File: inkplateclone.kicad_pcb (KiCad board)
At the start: 2 copper layers, 92 parts, among them J1 ED060SC7, J2 USB_C_Receptacle_USB2.0, J3 Conn_01x03_Male, J4 Conn_01x03_Male, J5 Conn_01x02_Male, Q1 Q_NMOS_GSD, Q2 Q_NMOS_GSD, Q3 Q_PMOS_GSD, SW1 SW_Push, SW2 SW_Push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

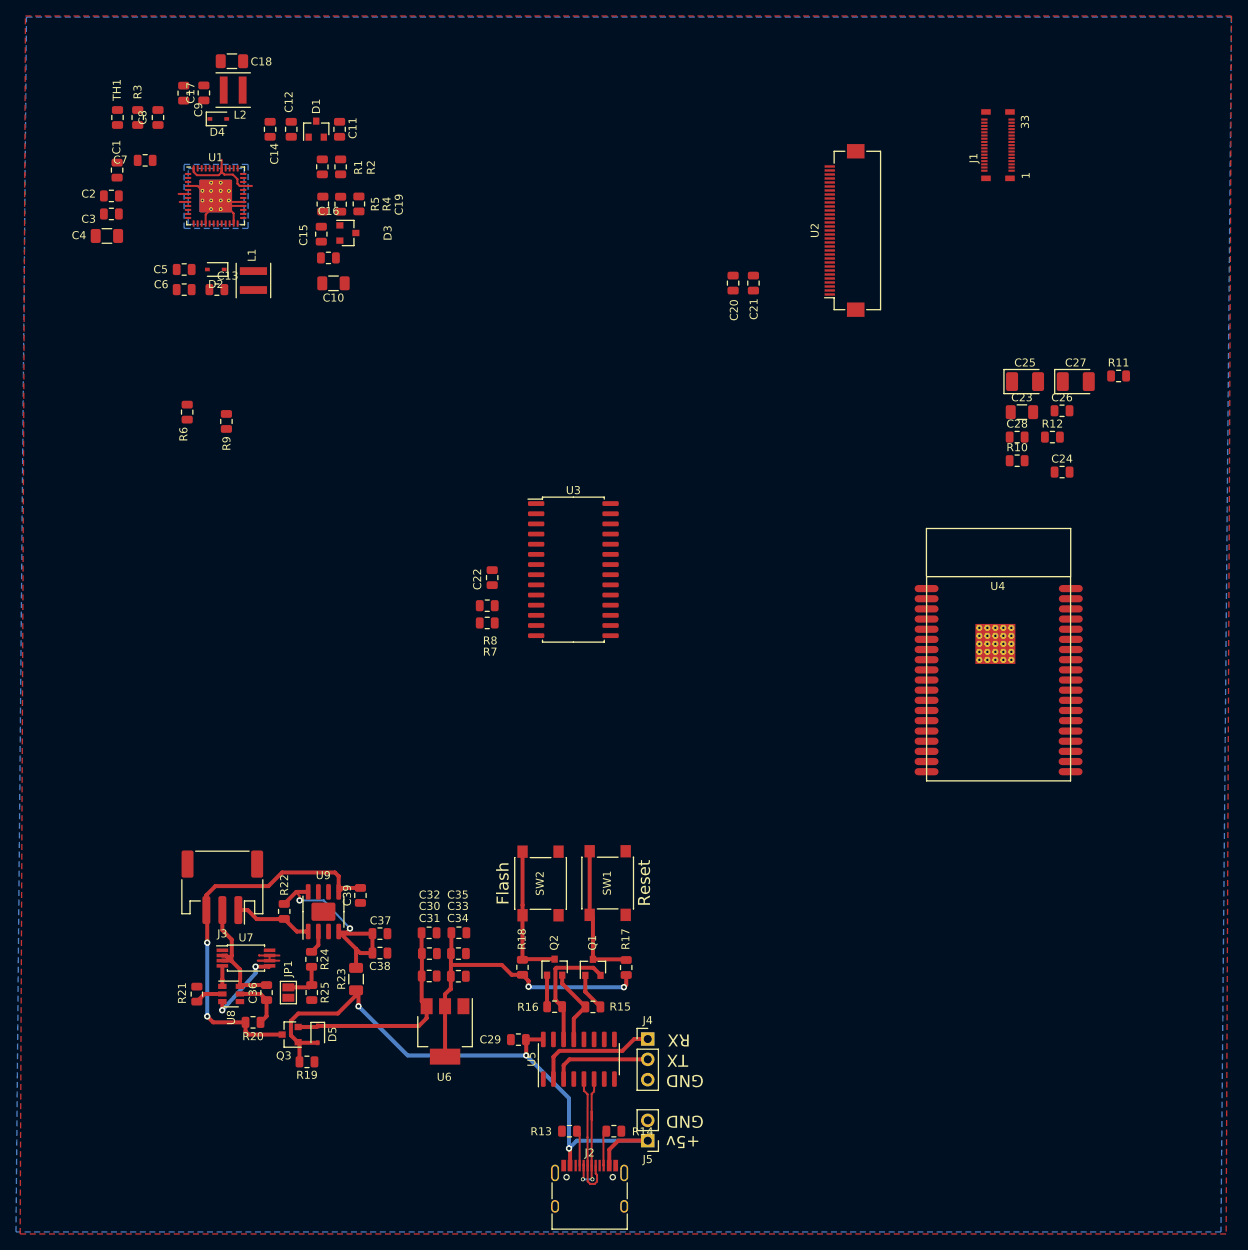
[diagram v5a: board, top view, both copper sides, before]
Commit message: added 3d models for the connectors. Not satisfied but they will do for now.
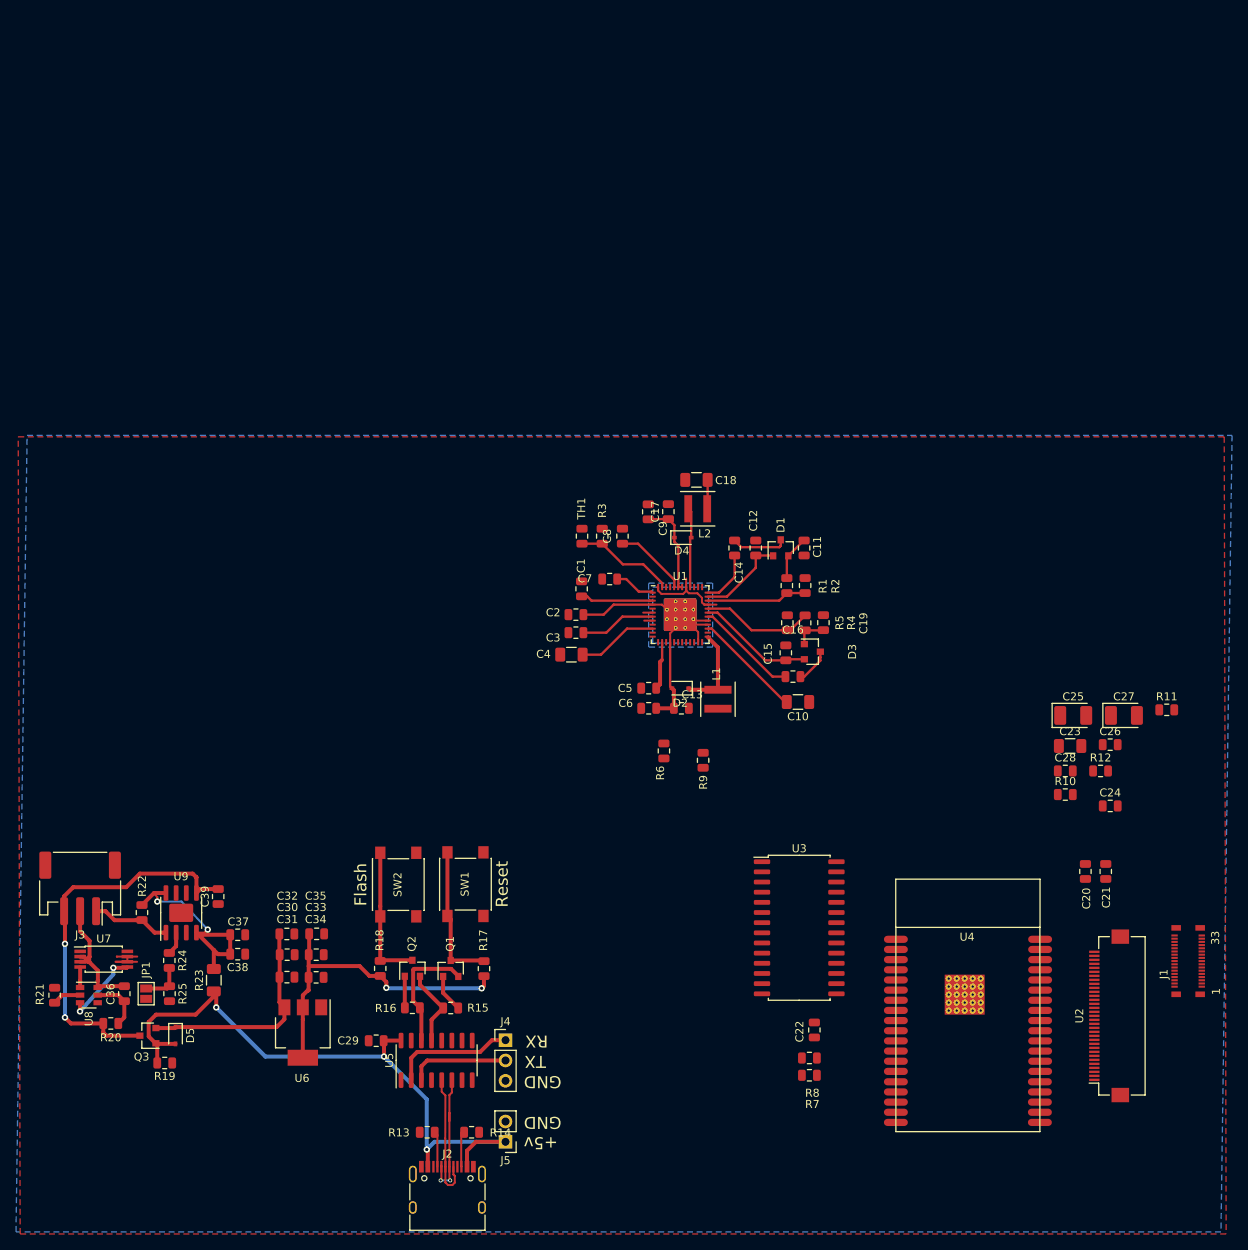
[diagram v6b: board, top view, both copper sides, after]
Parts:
- moved J1 104.7 mm to (186.7, 153.6)
- moved U2 103.6 mm to (176.9, 160.4)
- moved C20 85.7 mm to (173.9, 142.4)
- moved C21 85.7 mm to (176.4, 142.4)
- moved C10 78.2 mm to (138.0, 121.2)
- moved C11 78.2 mm to (138.7, 101.9)
- moved C12 78.2 mm to (130.0, 101.9)
- moved C14 78.2 mm to (132.7, 101.9)
- moved C17 78.2 mm to (121.8, 97.4)
- moved C3 78.2 mm to (110.2, 112.5)
- moved C7 78.2 mm to (114.4, 105.8)
- moved C9 78.2 mm to (119.3, 97.4)
- moved D3 78.2 mm to (139.8, 114.9)
- moved L1 78.2 mm to (128.0, 120.8)
- moved L2 78.2 mm to (125.4, 97.0)
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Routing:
- net VIN: track 27.5 -> 54.9 mm
- net /VN: track 13.0 -> 32.8 mm
- net /VEE_D: track 0.00 -> 14.6 mm
- net /VEE_FB: track 0.00 -> 14.1 mm
- net /VEE_DRV: track 0.00 -> 12.8 mm
- net /VDDH_FB: track 0.00 -> 12.6 mm
- net /TS: track 0.00 -> 12.5 mm
- net /VB: track 0.00 -> 12.0 mm
- net /VDDH_D: track 0.00 -> 11.2 mm
- net /VN_SW: track 0.00 -> 10.8 mm
- net /VB_SW: track 0.00 -> 9.99 mm
- net /INT_LDO: track 0.00 -> 9.47 mm
- net /VPOS: track 0.00 -> 9.27 mm
- net /VNEG: track 0.00 -> 9.09 mm
- net Net-(C12-Pad1): track 0.00 -> 6.93 mm
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
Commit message: opruimen
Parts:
- moved C1 36.8 mm to (74.2, 109.1)
- moved C11 36.8 mm to (102.0, 104.0)
- moved C12 36.8 mm to (93.3, 104.0)
- moved C14 36.8 mm to (96.0, 104.0)
- moved C15 36.8 mm to (99.7, 117.1)
- moved C17 36.8 mm to (85.0, 99.4)
- moved C18 36.8 mm to (88.5, 95.4)
- moved C5 36.8 mm to (82.6, 121.5)
- moved C6 36.8 mm to (82.6, 124.0)
- moved R9 36.8 mm to (89.4, 130.5)
- moved C10 36.8 mm to (101.2, 123.2)
- moved C13 36.8 mm to (86.7, 124.0)
- moved C16 36.8 mm to (100.6, 120.0)
- moved C19 36.8 mm to (104.4, 113.3)
- moved C2 36.8 mm to (73.5, 112.3)
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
